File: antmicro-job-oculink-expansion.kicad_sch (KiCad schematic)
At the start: 105 parts, among them J1 OCuLink_x4_Amphenol_G14A42121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, J2 Plug_Samtec_ERM8_2x40_ERM8-04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, U1 MAX3373EEKA+, U2 PI3EQX16904GL, U3 PI3EQX16904GL

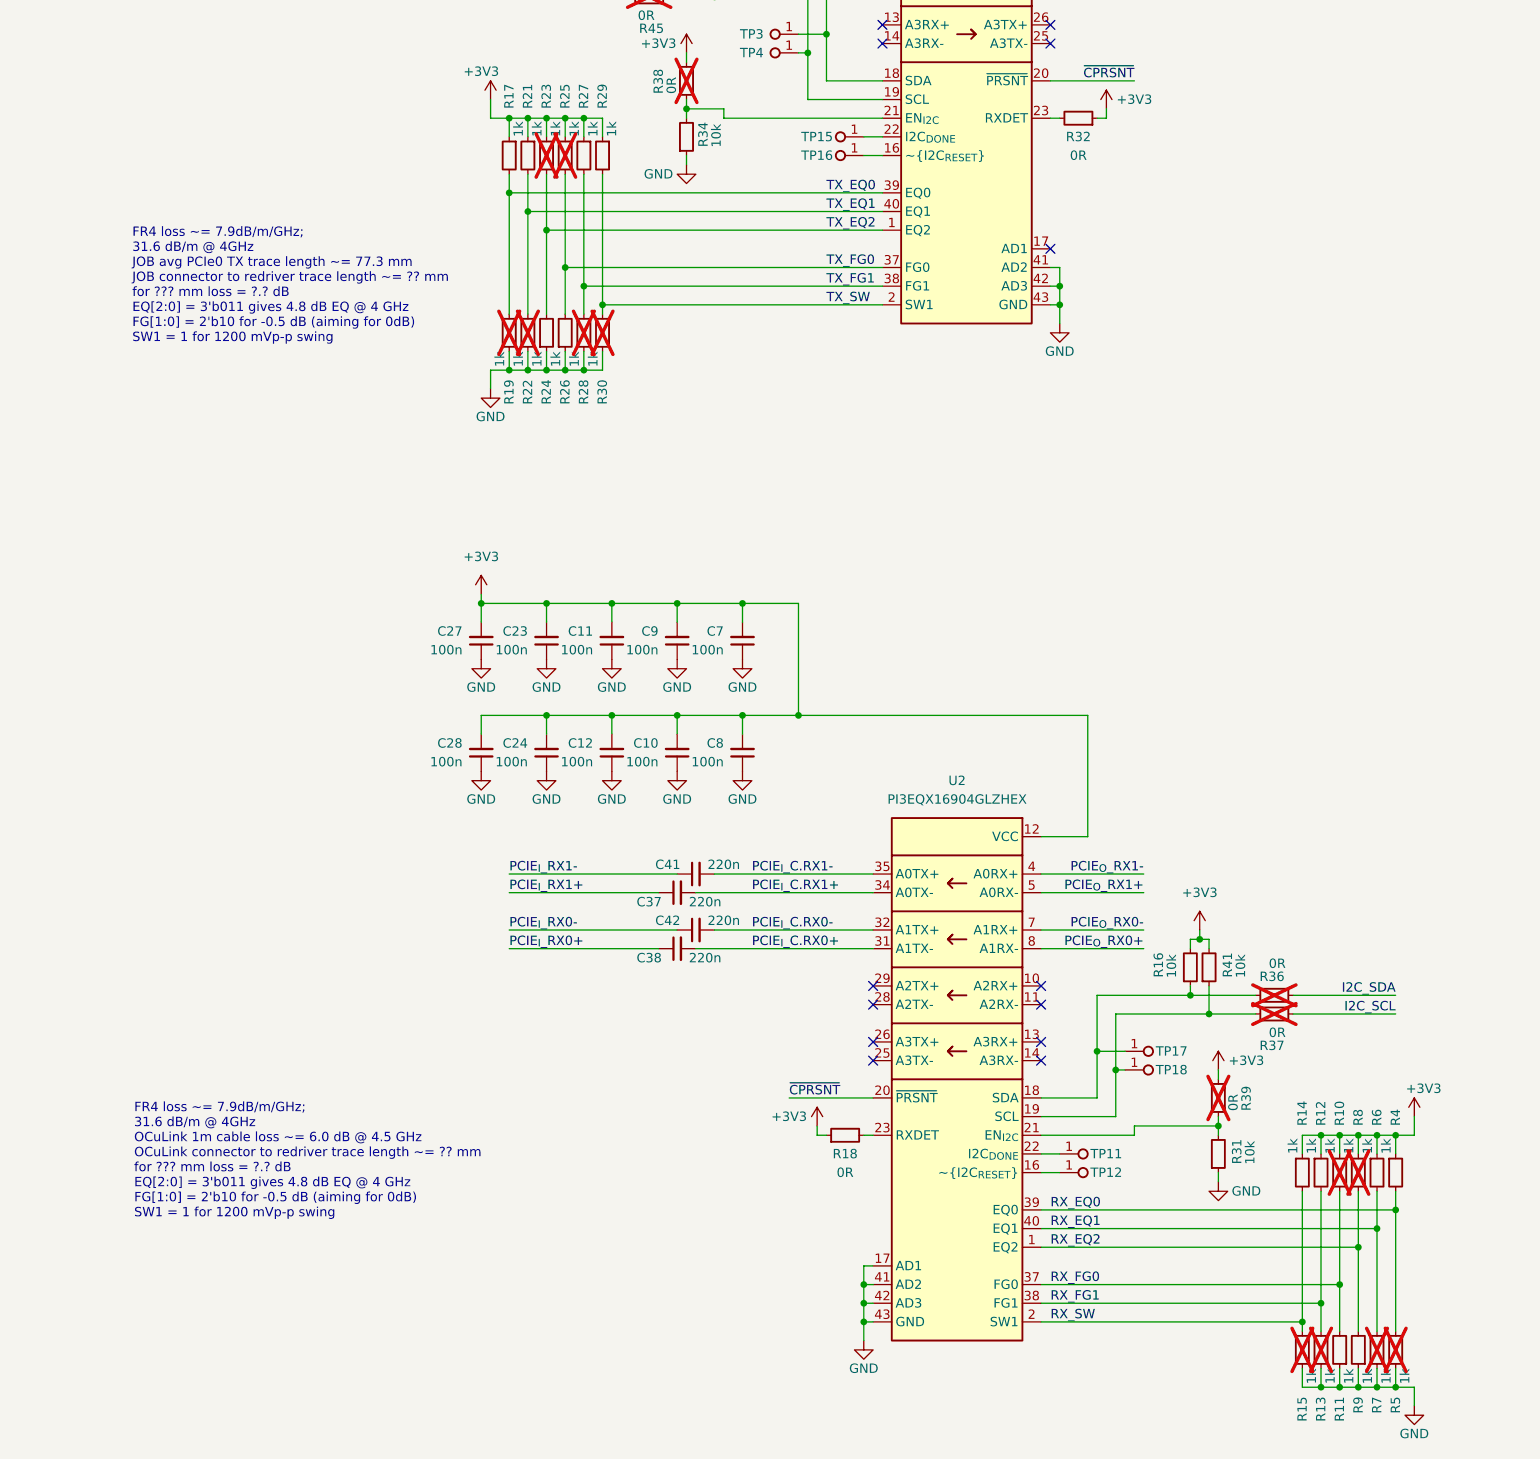
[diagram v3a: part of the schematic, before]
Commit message: [#76814] Configure the redrivers
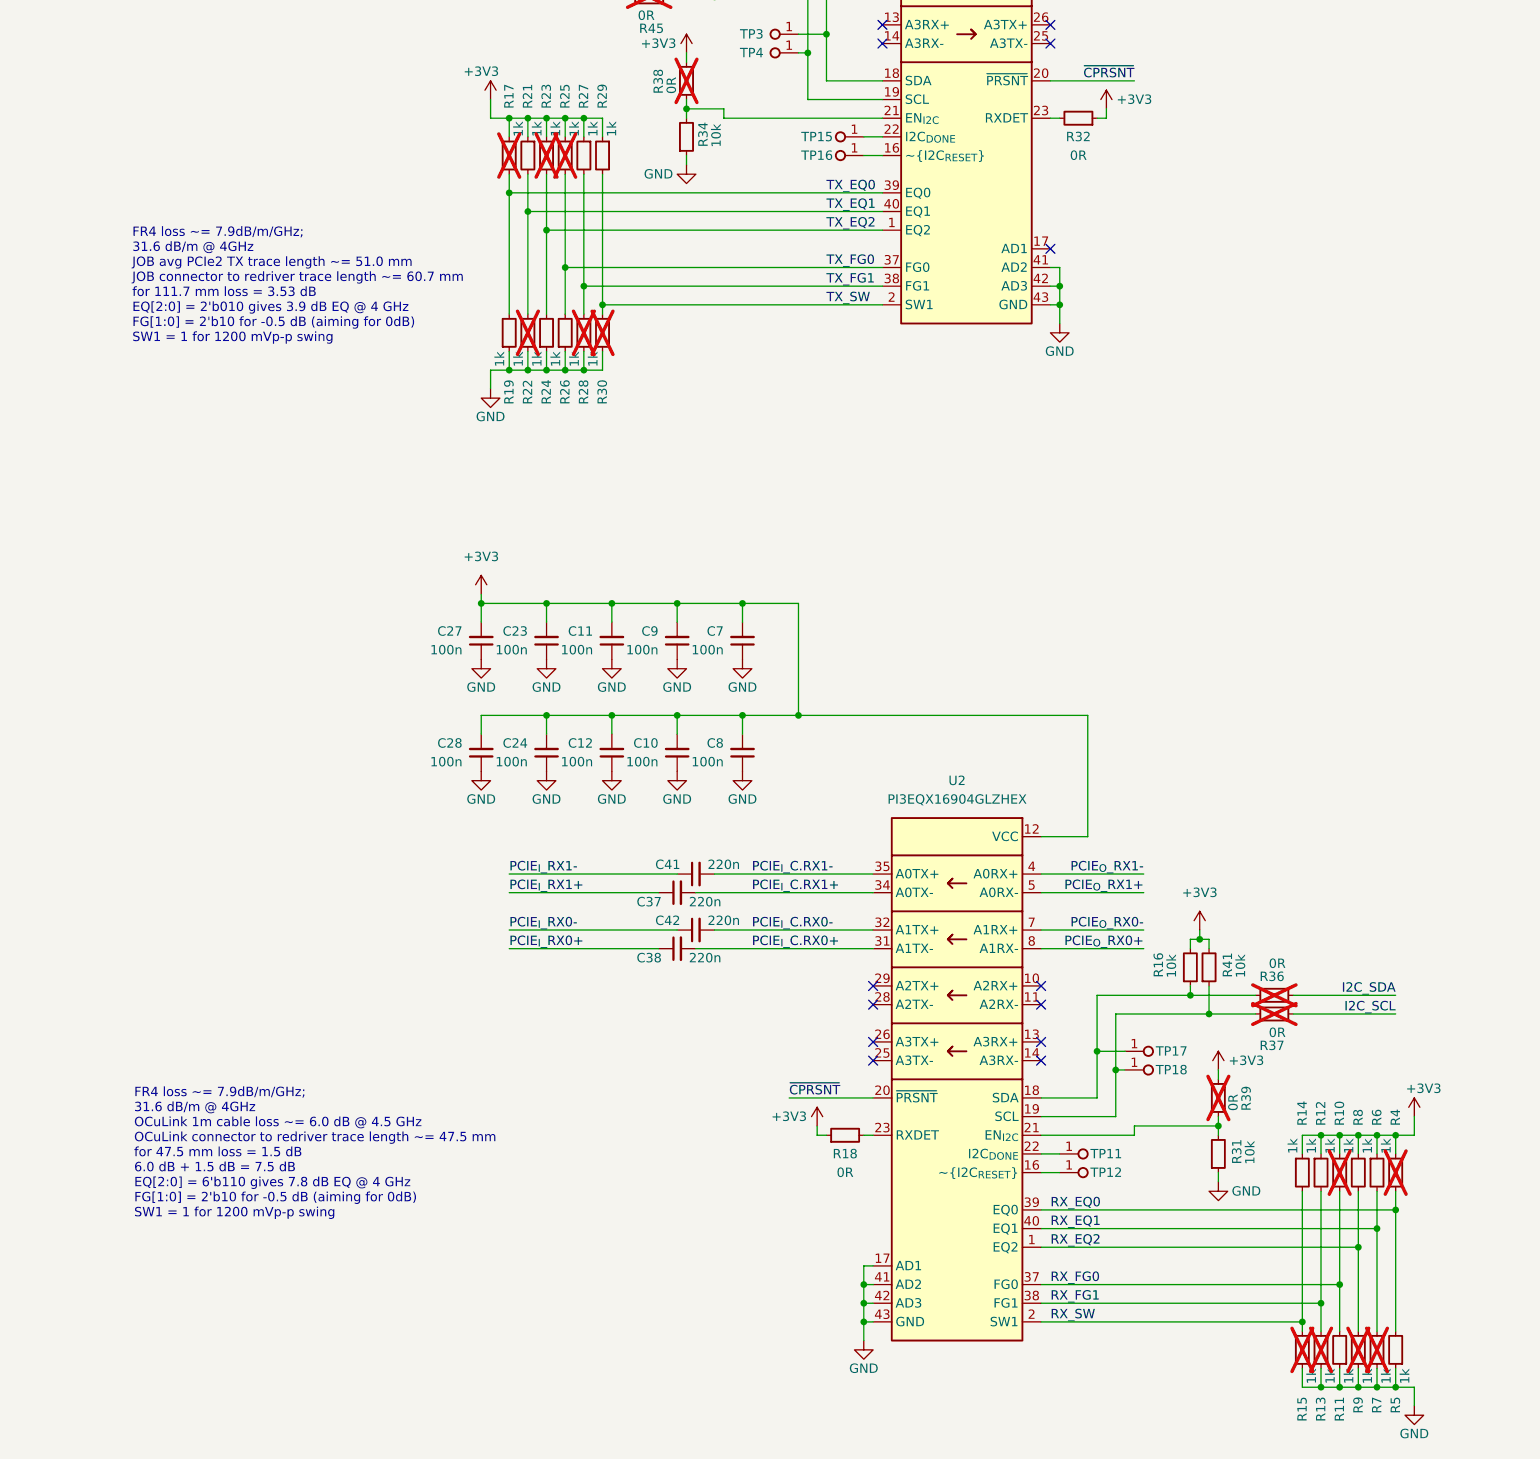
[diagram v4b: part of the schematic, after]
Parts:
- R17, R4, R9: now not fitted
- R19, R5, R8: now fitted
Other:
- note added: "FR4 loss ~= 7.9dB/m/GHz; 31.6 dB/m @ 4GHz JOB avg PCIe2 TX trace length ~= 51.0 mm JOB connector to redriver trace length ~= 60.7 mm for 111.7 mm loss = 3.53 dB EQ[2:0] = 2'b010 gives 3.9 dB EQ @ 4 GHz FG[1:0] = 2'b10 for -0.5 dB (aiming for 0dB) SW1 = 1 for 1200 mVp-p swing"
- note added: "FR4 loss ~= 7.9dB/m/GHz; 31.6 dB/m @ 4GHz OCuLink 1m cable loss ~= 6.0 dB @ 4.5 GHz OCuLink connector to redriver trace length ~= 47.5 mm for 47.5 mm loss = 1.5 dB 6.0 dB + 1.5 dB = 7.5 dB EQ[2:0] = 6'b110 gives 7.8 dB EQ @ 4 GHz FG[1:0] = 2'b10 for -0.5 dB (aiming for 0dB) SW1 = 1 for 1200 mVp-p swing"
- note removed: "FR4 loss ~= 7.9dB/m/GHz; 31.6 dB/m @ 4GHz JOB avg PCIe0 TX trace length ~= 77.3 mm JOB connector to redriver trace length ~= ?? mm for ??? mm loss = ?.? dB EQ[2:0] = 3'b011 gives 4.8 dB EQ @ 4 GHz FG[1:0] = 2'b10 for -0.5 dB (aiming for 0dB) SW1 = 1 for 1200 mVp-p swing"
- note removed: "FR4 loss ~= 7.9dB/m/GHz; 31.6 dB/m @ 4GHz OCuLink 1m cable loss ~= 6.0 dB @ 4.5 GHz OCuLink connector to redriver trace length ~= ?? mm for ??? mm loss = ?.? dB EQ[2:0] = 3'b011 gives 4.8 dB EQ @ 4 GHz FG[1:0] = 2'b10 for -0.5 dB (aiming for 0dB) SW1 = 1 for 1200 mVp-p swing"
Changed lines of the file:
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@@
 		)
 	)
-	(text "FR4 loss ~= 7.9dB/m/GHz; \n31.6 dB/m @ 4GHz\nJOB avg PCIe0 TX trace length ~= 77.3 mm\nJOB connector to redriver trace length ~= ?? mm\nfor ??? mm loss = ?.? dB\nEQ[2:0] = 3'b011 gives 4.8 dB EQ @ 4 GHz\nFG[1:0] = 2'b10 for -0.5 dB (aiming for 0dB)\nSW1 = 1 for 1200 mVp-p swing"
+	(text "FR4 loss ~= 7.9dB/m/GHz; \n31.6 dB/m @ 4GHz\nJOB avg PCIe2 TX trace length ~= 51.0 mm\nJOB connector to redriver trace length ~= 60.7 mm\nfor 111.7 mm loss = 3.53 dB\nEQ[2:0] = 2'b010 gives 3.9 dB EQ @ 4 GHz\nFG[1:0] = 2'b10 for -0.5 dB (aiming for 0dB)\nSW1 = 1 for 1200 mVp-p swing"
 		(exclude_from_sim no)
 		(at 98.552 129.794 0)
@@
 		)
 	)
-	(text "FR4 loss ~= 7.9dB/m/GHz; \n31.6 dB/m @ 4GHz\nOCuLink 1m cable loss ~= 6.0 dB @ 4.5 GHz\nOCuLink connector to redriver trace length ~= ?? mm\nfor ??? mm loss = ?.? dB\nEQ[2:0] = 3'b011 gives 4.8 dB EQ @ 4 GHz\nFG[1:0] = 2'b10 for -0.5 dB (aiming for 0dB)\nSW1 = 1 for 1200 mVp-p swing"
+	(text "FR4 loss ~= 7.9dB/m/GHz; \n31.6 dB/m @ 4GHz\nOCuLink 1m cable loss ~= 6.0 dB @ 4.5 GHz\nOCuLink connector to redriver trace length ~= 47.5 mm\nfor 47.5 mm loss = 1.5 dB\n6.0 dB + 1.5 dB = 7.5 dB\nEQ[2:0] = 6'b110 gives 7.8 dB EQ @ 4 GHz\nFG[1:0] = 2'b10 for -0.5 dB (aiming for 0dB)\nSW1 = 1 for 1200 mVp-p swing"
 		(exclude_from_sim no)
 		(at 98.806 248.92 0)
@@
 		(in_bom yes)
 		(on_board yes)
-		(dnp yes)
+		(dnp no)
 		(property "Reference" "R19"
 			(at 149.86 134.62 0)
@@
 		(in_bom yes)
 		(on_board yes)
-		(dnp no)
+		(dnp yes)
 		(property "Reference" "R9"
 			(at 265.43 273.05 0)
@@
 		(in_bom yes)
 		(on_board yes)
-		(dnp yes)
+		(dnp no)
 		(property "Reference" "R8"
 			(at 265.43 236.22 0)
@@
 		(in_bom yes)
 		(on_board yes)
-		(dnp no)
+		(dnp yes)
 		(property "Reference" "R4"
 			(at 270.51 236.22 0)
@@
 		(in_bom yes)
 		(on_board yes)
-		(dnp yes)
+		(dnp no)
 		(property "Reference" "R5"
 			(at 270.51 273.05 0)
@@
 		(in_bom yes)
 		(on_board yes)
-		(dnp no)
+		(dnp yes)
 		(property "Reference" "R17"
 			(at 149.86 97.79 0)

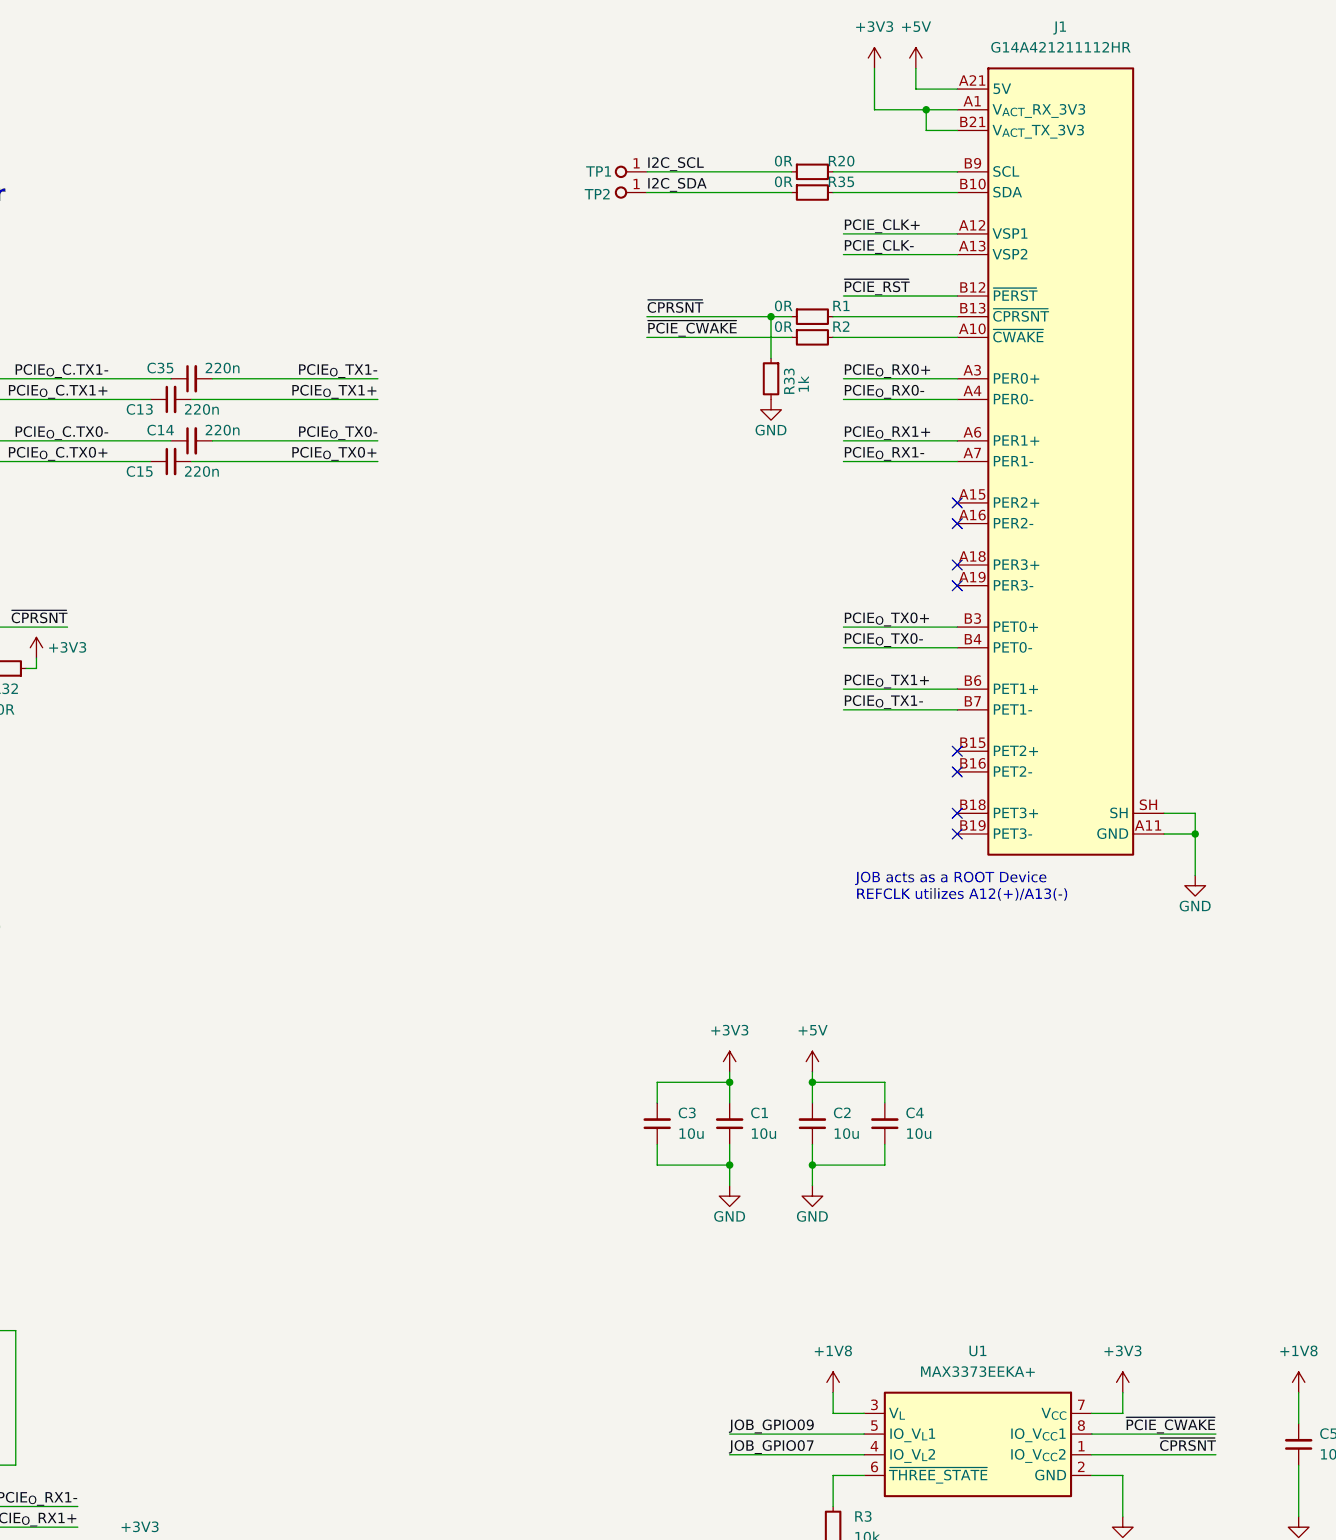
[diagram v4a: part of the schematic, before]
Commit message: [#77839] Add e-fuses to schematic
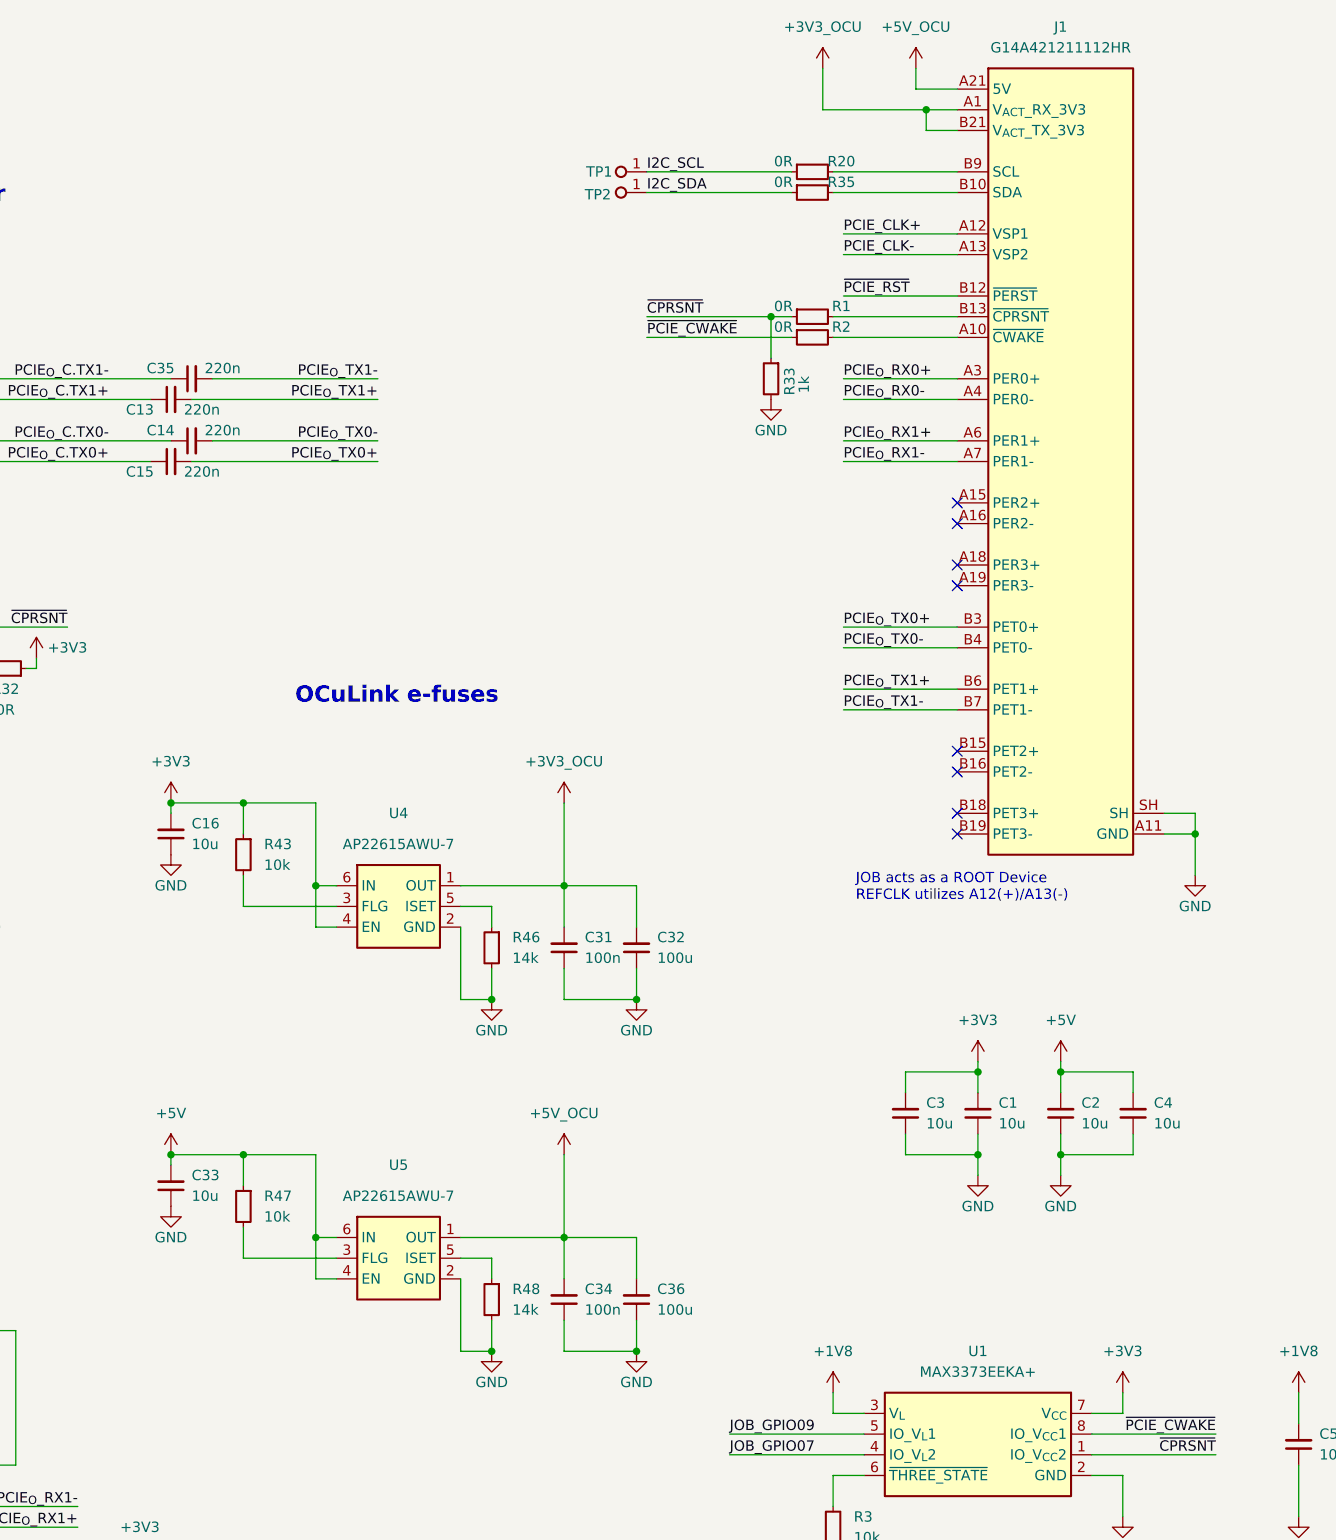
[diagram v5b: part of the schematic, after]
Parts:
- added C16, C33: C_10u_0402, antmicro-footprints:C_0402_1005Metric, symbol antmicroCapacitors0402:C_10u_0402
- added C31, C34: C_100n_0402, antmicro-footprints:C_0402_1005Metric, symbol antmicroCapacitors0402:C_100n_0402
- added C32, C36: C_100u_0805, antmicro-footprints:C_0805_2012Metric, symbol antmicroCapacitorsmisc:C_100u_0805
- added R43, R47: R_10k_0402, antmicro-footprints:R_0402_1005Metric, symbol antmicroResistors0402:R_10k_0402
- added R46, R48: R_14k_0402, antmicro-footprints:R_0402_1005Metric, symbol antmicroResistors0402:R_14k_0402
- added U4, U5: ~, antmicro-footprints:TSOT23-6, symbol antmicroPMICPowerDistributionSwitchesLoadDrivers:AP22615A_TSOT26
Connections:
- net +3V3: now also C16.2, R43.1, U4.4 (EN), U4.6 (IN); no longer J1.A1 (V_{ACT}_RX_3V3), J1.B21 (V_{ACT}_TX_3V3)
- net +5V: now also C33.2, R47.1, U5.4 (EN), U5.6 (IN); no longer J1.A21 (5V), J1.B1 (5V)
- net GND: now also C16.1, C31.1, C32.1, C33.1, C34.1, C36.1, R46.2, R48.2, U4.2 (GND), U5.2 (GND)
- new net: R43.2, U4.3 (FLG)
- new net: R48.1, U5.5 (ISET)
- new net: R47.2, U5.3 (FLG)
- new net: R46.1, U4.5 (ISET)
- new net +3V3_OCU: C31.2, C32.2, J1.A1 (V_{ACT}_RX_3V3), J1.B21 (V_{ACT}_TX_3V3), U4.1 (OUT)
- new net +5V_OCU: C34.2, C36.2, J1.A21 (5V), J1.B1 (5V), U5.1 (OUT)
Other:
- note added: "OCuLink e-fuses"
- moved on the sheet: C1, C2, C3, C4
